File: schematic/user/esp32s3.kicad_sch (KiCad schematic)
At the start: 12 parts, among them J4 I2C Breakout, SW1 ESP32S3 Reset, SW2 ESP32S3 Boot Method, U5 ESP32-S3-WROOM-1-N16R8

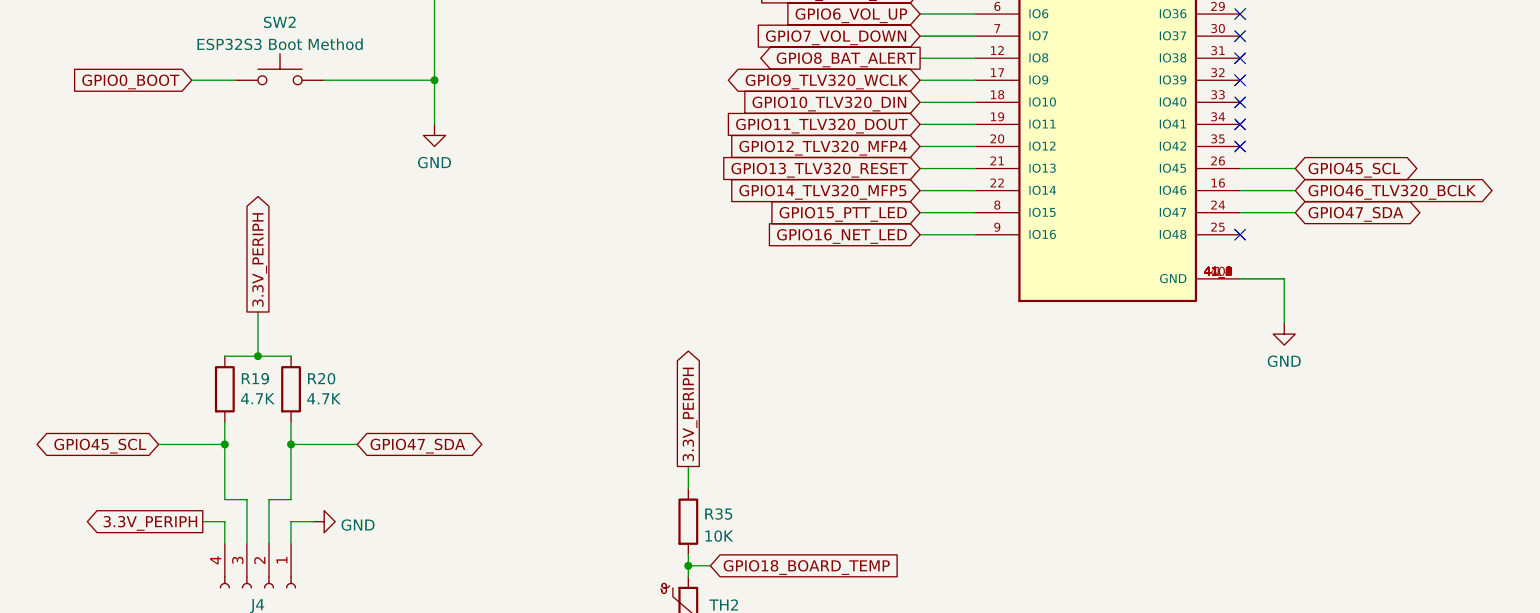
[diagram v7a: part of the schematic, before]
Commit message: v0.5 board: move SCL to GPIO 48 as 45 is a ESP32 strapping pin.
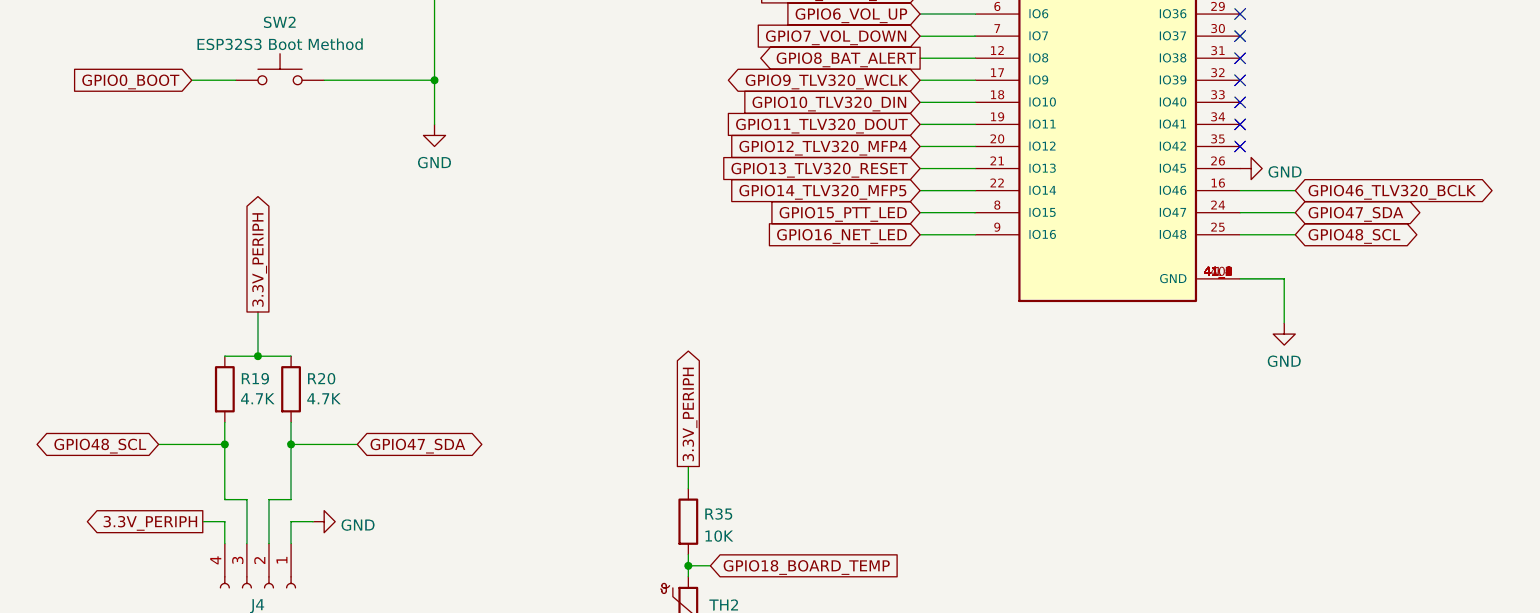
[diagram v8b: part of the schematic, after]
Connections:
- net GND: now also U5.26 (IO45)
- net GPIO48_SCL: now reaches U5.25 (IO48)
- net GPIO48_SCL: now also J4.3 (Pin_3), R19.2
- removed net GPIO45_SCL: J4.3 (Pin_3), R19.2, U5.26 (IO45)
- no-connect marks 11 -> 10
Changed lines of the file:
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@@
   (junction (at 124.46 163.83) (diameter 0) (color 0 0 0 0)
   )
-  (no_connect (at 187.96 125.73))
   (no_connect (at 187.96 107.95))
   (no_connect (at 187.96 105.41))
@@
   (no_connect (at 187.96 100.33))
   (no_connect (at 187.96 97.79))
-  (wire (pts (xy 187.96 118.11) (xy 194.31 118.11))
-    (stroke (width 0) (type default) (color 0 0 0 0))
-  )
   (wire (pts (xy 151.13 100.33) (xy 157.48 100.33))
     (stroke (width 0) (type default) (color 0 0 0 0))
@@
     (stroke (width 0) (type default) (color 0 0 0 0))
   )
+  (wire (pts (xy 187.96 125.73) (xy 194.31 125.73))
+    (stroke (width 0) (type default) (color 0 0 0 0))
+  )
   (wire (pts (xy 86.36 58.42) (xy 86.36 60.96))
     (stroke (width 0) (type default) (color 0 0 0 0))
@@
     )
   )
-  (global_label "GPIO45_SCL" (shape bidirectional) (at 194.31 118.11 0) (fields_autoplaced)
-    (effects (font (size 1.27 1.27)) (justify left))
-    (property "Intersheet References" "${INTERSHEET_REFS}" (id 0) (at 208.0926 118.0306 0)
+  (global_label "GPIO48_SCL" (shape bidirectional) (at 194.31 125.73 0) (fields_autoplaced)
+    (effects (font (size 1.27 1.27)) (justify left))
+    (property "Intersheet References" "${INTERSHEET_REFS}" (id 0) (at 208.0926 125.6506 0)
       (effects (font (size 1.27 1.27)) (justify left) hide)
     )
@@
     )
   )
-  (global_label "GPIO45_SCL" (shape bidirectional) (at 63.5 149.86 180) (fields_autoplaced)
+  (global_label "GPIO48_SCL" (shape bidirectional) (at 63.5 149.86 180) (fields_autoplaced)
     (effects (font (size 1.27 1.27)) (justify right))
     (property "Intersheet References" "${INTERSHEET_REFS}" (id 0) (at 49.7174 149.7806 0)
@@
     (pin "2")
   )
+  (symbol (lib_id "power:GND") (at 187.96 118.11 90) (unit 1)
+    (in_bom yes) (on_board yes) (fields_autoplaced)
+    (property "Reference" "#PWR0104" (id 0) (at 194.31 118.11 0)
+      (effects (font (size 1.27 1.27)) hide)
+    )
+    (property "Value" "GND" (id 1) (at 191.135 118.5438 90)
+      (effects (font (size 1.27 1.27)) (justify right))
+    )
+    (property "Footprint" "" (id 2) (at 187.96 118.11 0)
+      (effects (font (size 1.27 1.27)) hide)
+    )
+    (property "Datasheet" "" (id 3) (at 187.96 118.11 0)
+      (effects (font (size 1.27 1.27)) hide)
+    )
+    (pin "1")
+  )
   (symbol (lib_id "Connector:Conn_01x04_Female") (at 76.2 166.37 270) (unit 1)
